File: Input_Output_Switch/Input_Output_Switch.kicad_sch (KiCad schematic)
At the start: 34 parts, among them J1 RV, J2 AudioJackIn, J3 AudioJackOut, J4 Barrel_Jack_Switch, J5 Gain, J8 PWR, U1 TL072

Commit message: Final version 1.0 ordered
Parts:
- J1: value RV -> B3B-XH-A; footprint Connector_PinHeader_2.54mm:PinHeader_1x03_P2.54mm_Horizontal -> Connector_JST:JST_XH_B3B-XH-A_1x03_P2.50mm_Vertical; URL (none) -> https://www.digikey.com/en/products/detail/jst-sales-americ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
- J2: value AudioJackIn -> A-6730
- J3: value AudioJackOut -> A-6730
- J4: value Barrel_Jack_Switch -> A-4118; URL (none) -> https://www.taydaelectronics.com/dc-power-jack-2-1mm-barrel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
- J8: value PWR -> B3B-XH-A; footprint Connector_PinHeader_2.54mm:PinHeader_1x03_P2.54mm_Vertical -> Connector_JST:JST_XH_B3B-XH-A_1x03_P2.50mm_Vertical; URL (none) -> https://www.digikey.com/en/products/detail/jst-sales-americ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
- POT1: renamed from RV1; value 10K -> A-4728; Alt2 https://www.taydaelectronics.com/potentiometer-variable-res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 -> (none)
- TP10, TP11, TP7, TP9, TPG1, TPG2: now left out of the parts list
- U1: value TL072 -> 296-TL072HIDRCT-ND
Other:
- title: (none) -> EQ8-Main-Board

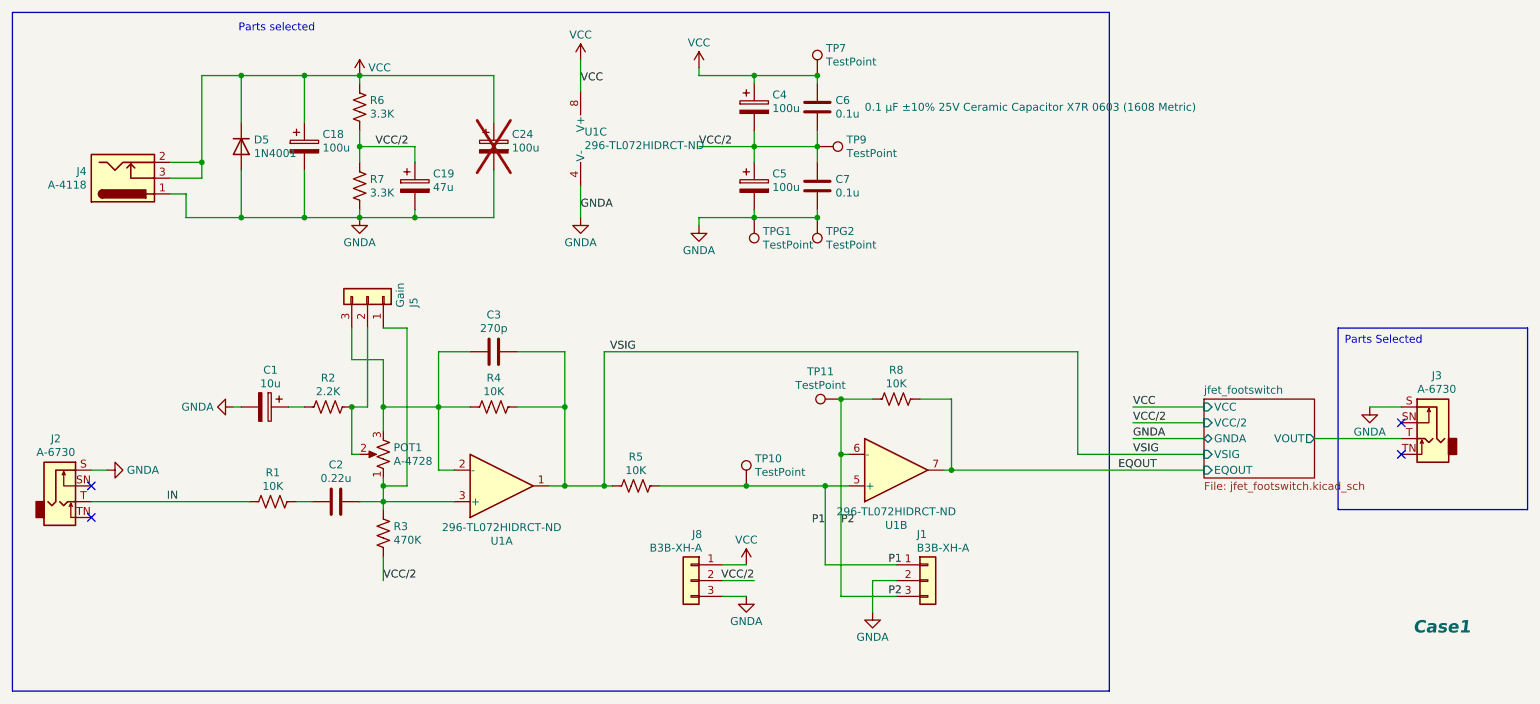
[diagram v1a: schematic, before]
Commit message: Fix bypass resistor, add missing Vcc. Move to Kicad-9
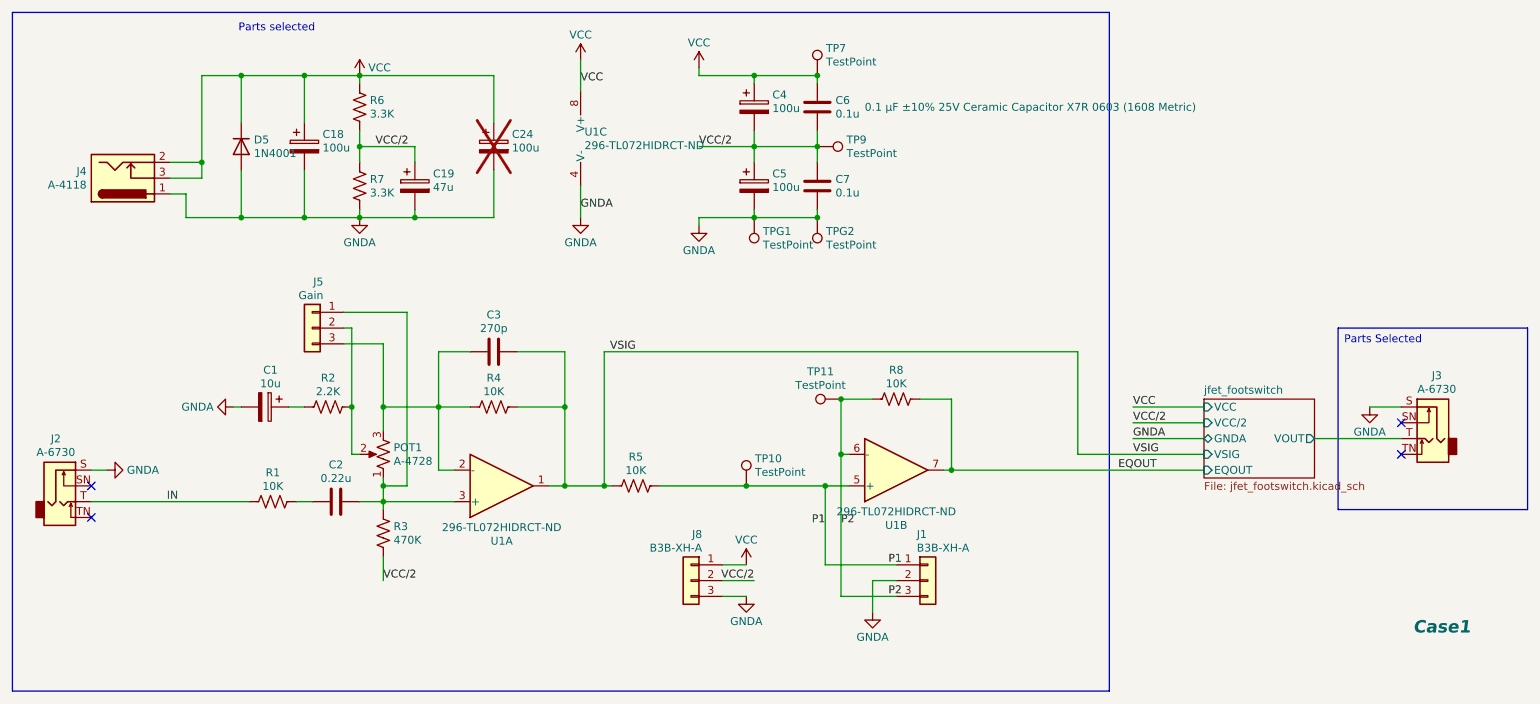
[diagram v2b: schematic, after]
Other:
- moved on the sheet: J5
